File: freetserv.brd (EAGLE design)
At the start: 91.4 x 82.5 mm, 157 parts, among them IC1 MCP16311-E/MS, IC10 MAX3232ECPW, IC11 MAX3232ECPW, IC12 MAX3232ECPW, IC13 MAX3232ECPW, IC14 FT4232HL, IC15 MAX3232ECPW, IC16 MAX3232ECPW, IC17 MAX3232ECPW, IC18 MAX3232ECPW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

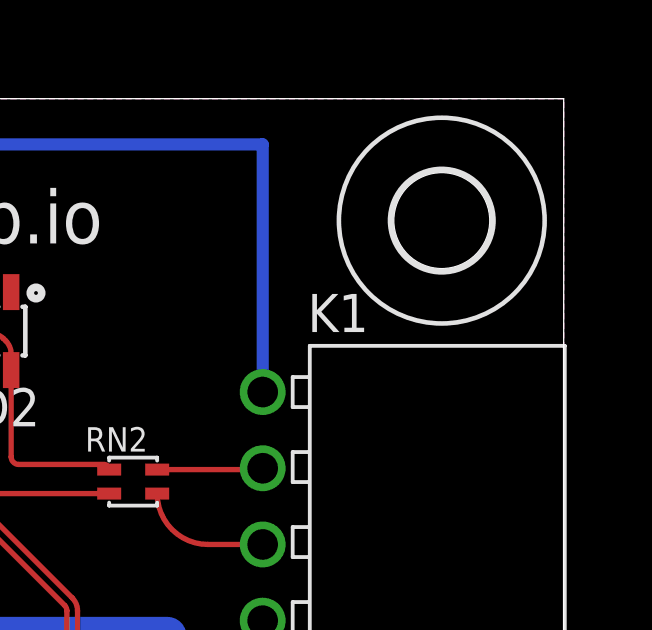
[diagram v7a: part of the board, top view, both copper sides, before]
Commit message: update part numbers and BOM
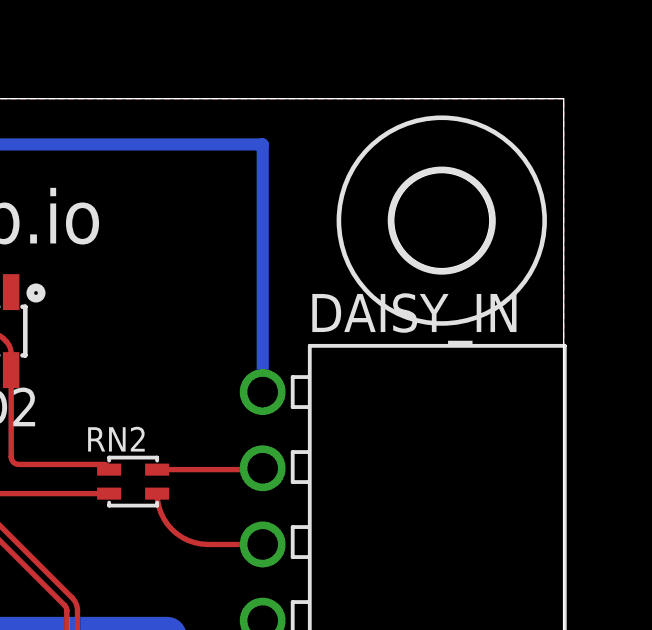
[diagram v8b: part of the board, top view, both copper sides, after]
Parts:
- renumbered K1 to DAISY_IN
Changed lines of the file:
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@@
 <element name="H1" library="holes" package="3,2" value="MOUNT-HOLE3.2" x="4.064" y="78.486"/>
 <element name="H2" library="holes" package="3,2" value="MOUNT-HOLE3.2" x="87.376" y="78.486"/>
-<element name="RN2" library="resistor-net" package="EXBV4V" value="27" x="77.089" y="69.7865" rot="R270"/>
-<element name="D1" library="texas1" package="SOT23-6" value="SN65220" x="36.449" y="71.9455" rot="R270"/>
-<element name="D2" library="texas1" package="SOT23-6" value="SN65220" x="72.0725" y="74.803" rot="R180"/>
-<element name="QG1" library="crystal" package="XO53" value="ASV-12.000MHZ-EJ-T" x="66.167" y="60.198" rot="MR180"/>
+<element name="RN2" library="resistor-net" package="EXBV4V" value="27" x="77.089" y="69.7865" rot="R270">
+<attribute name="PARTNO" value="Y2270CT-ND" x="77.089" y="69.7865" size="1.778" layer="27" rot="R270" display="off"/>
+</element>
+<element name="D1" library="texas1" package="SOT23-6" value="SN65220" x="36.449" y="71.9455" rot="R270">
+<attribute name="PARTNO" value="296-9694-1-ND" x="36.449" y="71.9455" size="1.778" layer="27" rot="R270" display="off"/>
+</element>
+<element name="D2" library="texas1" package="SOT23-6" value="SN65220" x="72.0725" y="74.803" rot="R180">
+<attribute name="PARTNO" value="296-9694-1-ND" x="72.0725" y="74.803" size="1.778" layer="27" rot="R180" display="off"/>
+</element>
+<element name="QG1" library="crystal" package="XO53" value="ASV-12.000MHZ-EJ-T" x="66.167" y="60.198" rot="MR180">
+<attribute name="PARTNO" value="535-9309-1-ND" x="66.167" y="60.198" size="1.778" layer="28" rot="MR180" display="off"/>
+</element>
 <element name="C47" library="resistor" package="C0805" value="0.1uF" x="62.357" y="60.325" rot="MR90">
 <attribute name="PARTNO" value="1276-1003-1-ND" x="62.357" y="60.325" size="1.778" layer="28" rot="MR90" display="off"/>
 </element>
-<element name="PWRIN" library="pinhead" package="1X02" value="" x="14.859" y="79.756" rot="R270"/>
-<element name="DAISY_OUT" library="Wurth_Elektronik_Electromechanic_Board_to_Board_Connectors_rev15c" package="61300411021" value="61300411021" x="5.207" y="68.834" rot="R90"/>
-<element name="K1" library="Wurth_Elektronik_Electromechanic_Board_to_Board_Connectors_rev15c" package="613004143121" value="613004143121" x="81.407" y="72.771" rot="R270"/>
+<element name="PWRIN" library="pinhead" package="1X02" value="" x="14.859" y="79.756" rot="R270">
+<attribute name="PARTNO" value="A1921-ND" x="14.859" y="79.756" size="1.778" layer="27" rot="R270" display="off"/>
+</element>
+<element name="DAISY_OUT" library="Wurth_Elektronik_Electromechanic_Board_to_Board_Connectors_rev15c" package="61300411021" value="61300411021" x="5.207" y="68.834" rot="R90">
+<attribute name="PARTNO" value="732-5337-ND" x="5.207" y="68.834" size="1.778" layer="27" rot="R90" display="off"/>
+</element>
+<element name="DAISY_IN" library="Wurth_Elektronik_Electromechanic_Board_to_Board_Connectors_rev15c" package="613004143121" value="613004143121" x="81.407" y="72.771" rot="R270">
+<attribute name="PARTNO" value="732-2863-ND" x="81.407" y="72.771" size="1.778" layer="27" rot="R270" display="off"/>
+</element>
 <element name="R1" library="resistor" package="R0805" value="27" x="31.369" y="72.771" rot="R90">
-<attribute name="PARTNO" value="311-1.5KARCT-ND" x="31.369" y="72.771" size="1.778" layer="27" rot="R90" display="off"/>
+<attribute name="PARTNO" value="311-27ARCT-ND" x="31.369" y="72.771" size="1.778" layer="27" rot="R90" display="off"/>
 </element>
 <element name="R8" library="resistor" package="R0805" value="27" x="30.48" y="75.5015" rot="R180">
-<attribute name="PARTNO" value="311-1.5KARCT-ND" x="30.48" y="75.5015" size="1.778" layer="27" rot="R180" display="off"/>
+<attribute name="PARTNO" value="311-27ARCT-ND" x="30.48" y="75.5015" size="1.778" layer="27" rot="R180" display="off"/>
 </element>
 </elements>
@@
 <contactref element="IC1" pad="3"/>
 <contactref element="PWRIN" pad="1"/>
-<contactref element="K1" pad="1"/>
+<contactref element="DAISY_IN" pad="1"/>
 <contactref element="DAISY_OUT" pad="1"/>
 <wire x1="14.859" y1="81.026" x2="16.891" y2="81.026" width="0.4064" layer="16"/>
@@
 <signal name="N$7">
 <contactref element="RN2" pad="A2"/>
-<contactref element="K1" pad="2"/>
+<contactref element="DAISY_IN" pad="2"/>
 <wire x1="77.889" y1="70.1865" x2="81.407" y2="70.1865" width="0.1778" layer="1"/>
 <wire x1="81.407" y1="70.1865" x2="81.407" y2="70.231" width="0.1778" layer="1"/>
@@
 <signal name="N$8">
 <contactref element="RN2" pad="B2"/>
-<contactref element="K1" pad="3"/>
+<contactref element="DAISY_IN" pad="3"/>
 <wire x1="77.889" y1="69.3865" x2="79.5845" y2="67.691" width="0.1778" layer="1" curve="90"/>
 <wire x1="79.5845" y1="67.691" x2="81.407" y2="67.691" width="0.1778" layer="1"/>
 </signal>
 <signal name="N$15">
-<contactref element="K1" pad="4"/>
+<contactref element="DAISY_IN" pad="4"/>
 </signal>
 <signal name="N$16">
